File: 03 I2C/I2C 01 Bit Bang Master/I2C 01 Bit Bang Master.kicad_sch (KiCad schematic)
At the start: 19 parts, among them J101 ICSP, J102 USB_A, SW101 SW_DIP_x08, U101 PIC18F47Q43-I/PT, U102 MCP23017_SO, U103 FT232RL

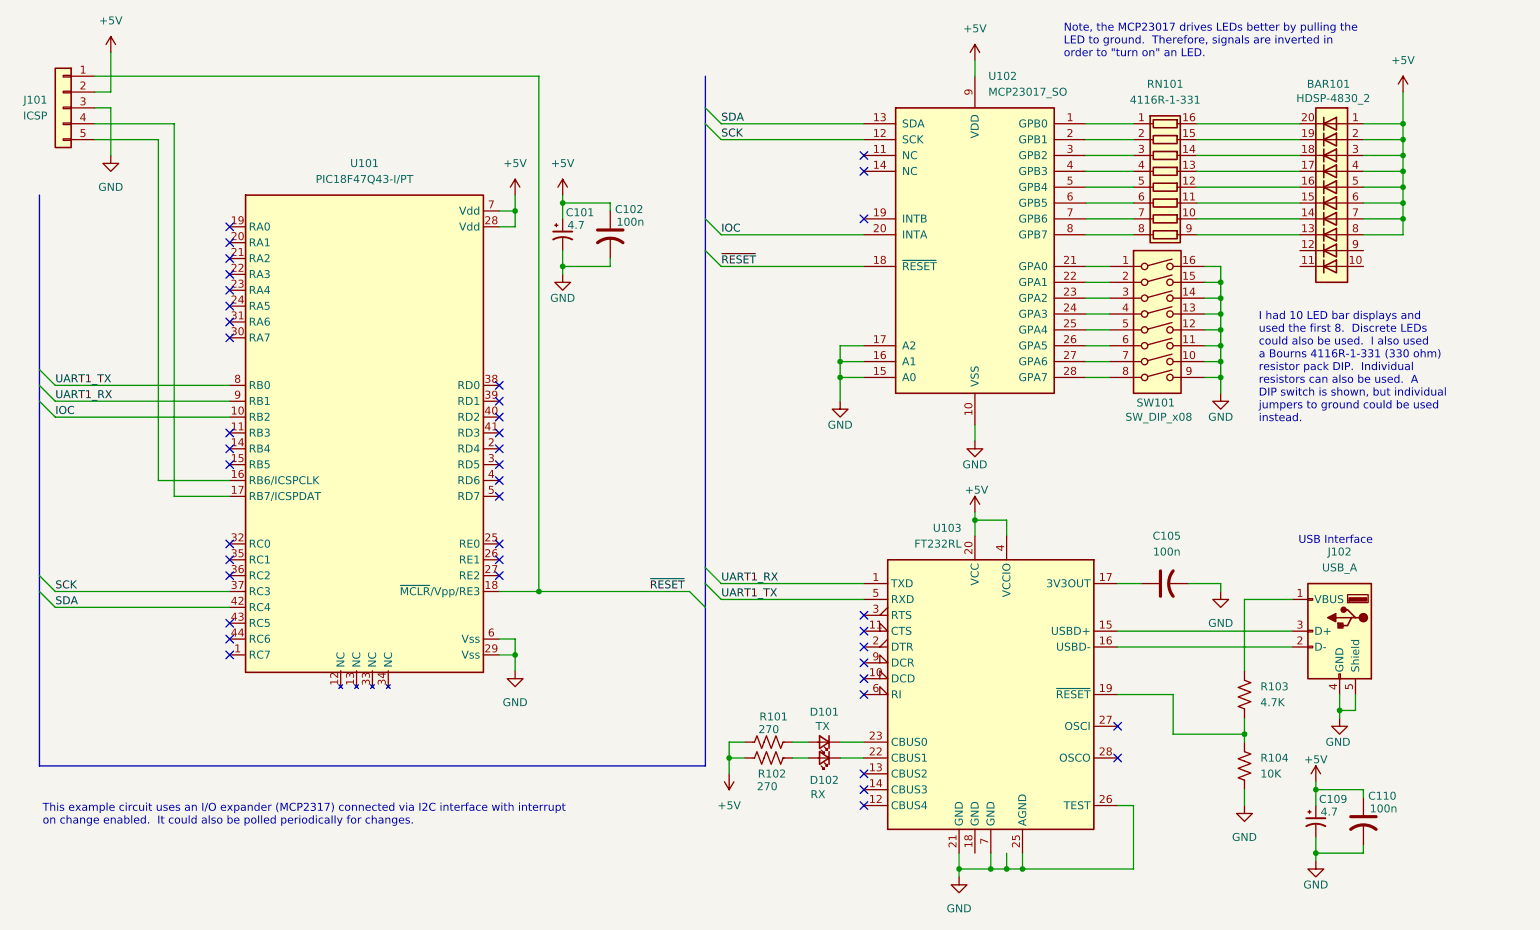
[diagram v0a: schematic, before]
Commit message: update schematic
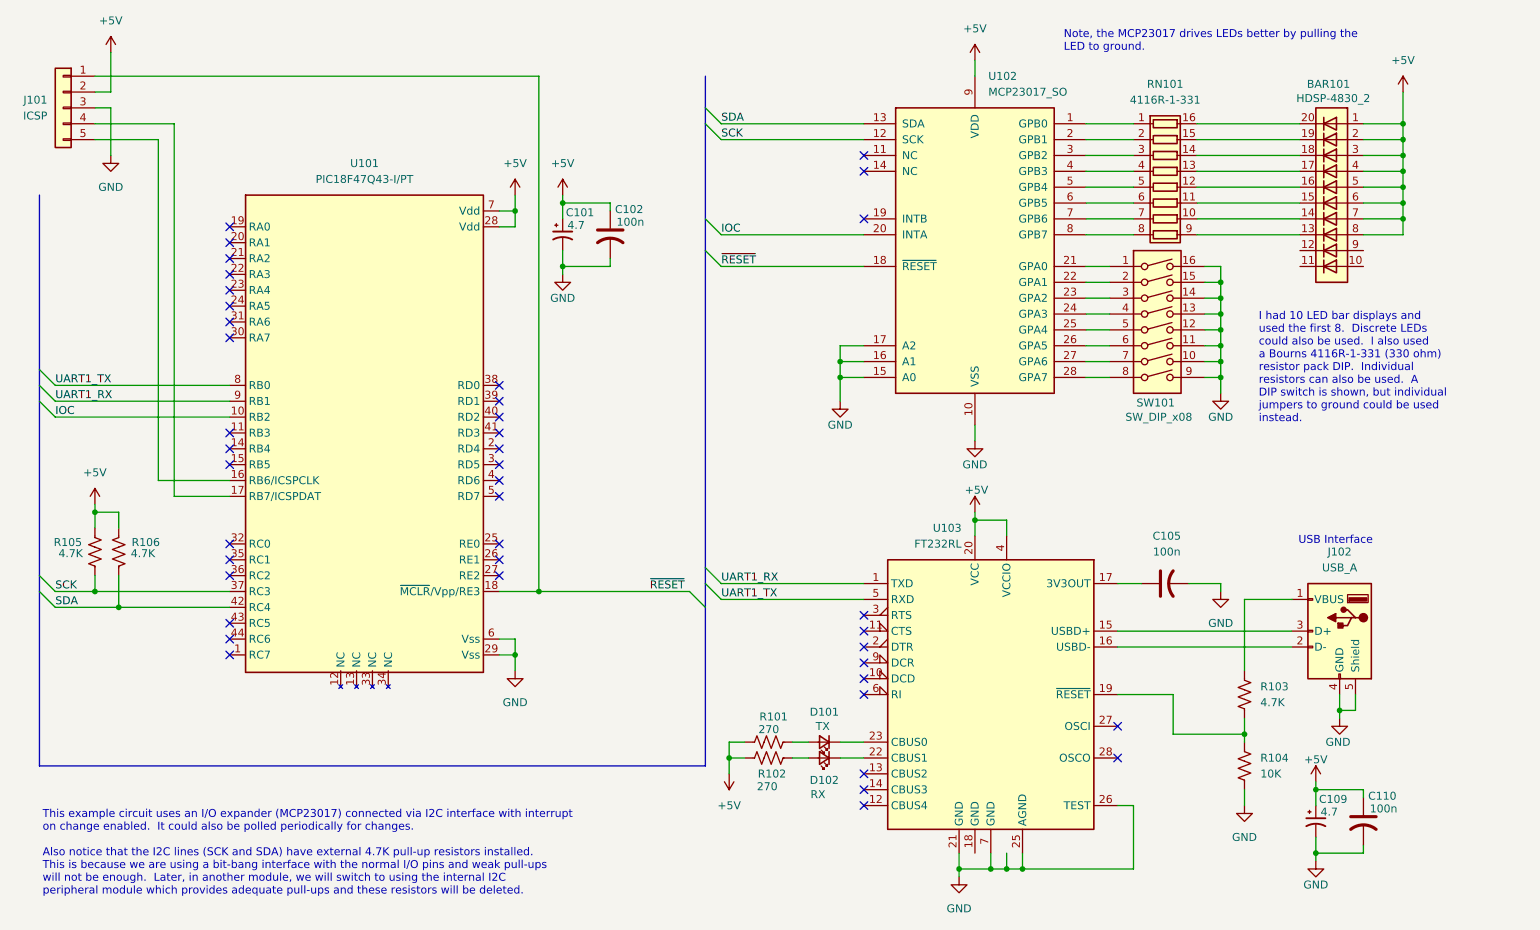
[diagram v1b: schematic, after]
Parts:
- added R105, R106: 4.7K, symbol Device:R_US
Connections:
- net +5V: now also R105.1, R106.1
- net SCK: now also R105.2
- net SDA: now also R106.2
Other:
- note added: "Note, the MCP23017 drives LEDs better by pulling the LED to ground."
- note added: "This example circuit uses an I/O expander (MCP23017) connected via I2C interface with interrupt on change enabled. It could also be polled periodically for changes. Also notice that the I2C lines (SCK and SDA) have external 4.7K pull-up resistors installed. This is because we are using a bit-bang interface with the normal I/O pins and weak pull-ups will not be enough. Later, in another module, we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"
- note removed: "Note, the MCP23017 drives LEDs better by pulling the LED to ground. Therefore, signals are inverted in order to "turn on" an LED."
- note removed: "This example circuit uses an I/O expander (MCP2317) connected via I2C interface with interrupt on change enabled. It could also be polled periodically for changes."
